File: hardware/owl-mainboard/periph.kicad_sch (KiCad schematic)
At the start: 38 parts, among them J301 AMOLED FPC, J302 LRA, J303 DOCK: GND, VBUS, DET, GND, U301 DRV2605LDGSR, U302 TMAG5273A2QDBVR, U303 LIS2DW12TR, U304 OPT3001DNPR, U305 LSF0204PWR, U306 XC6206P182MR

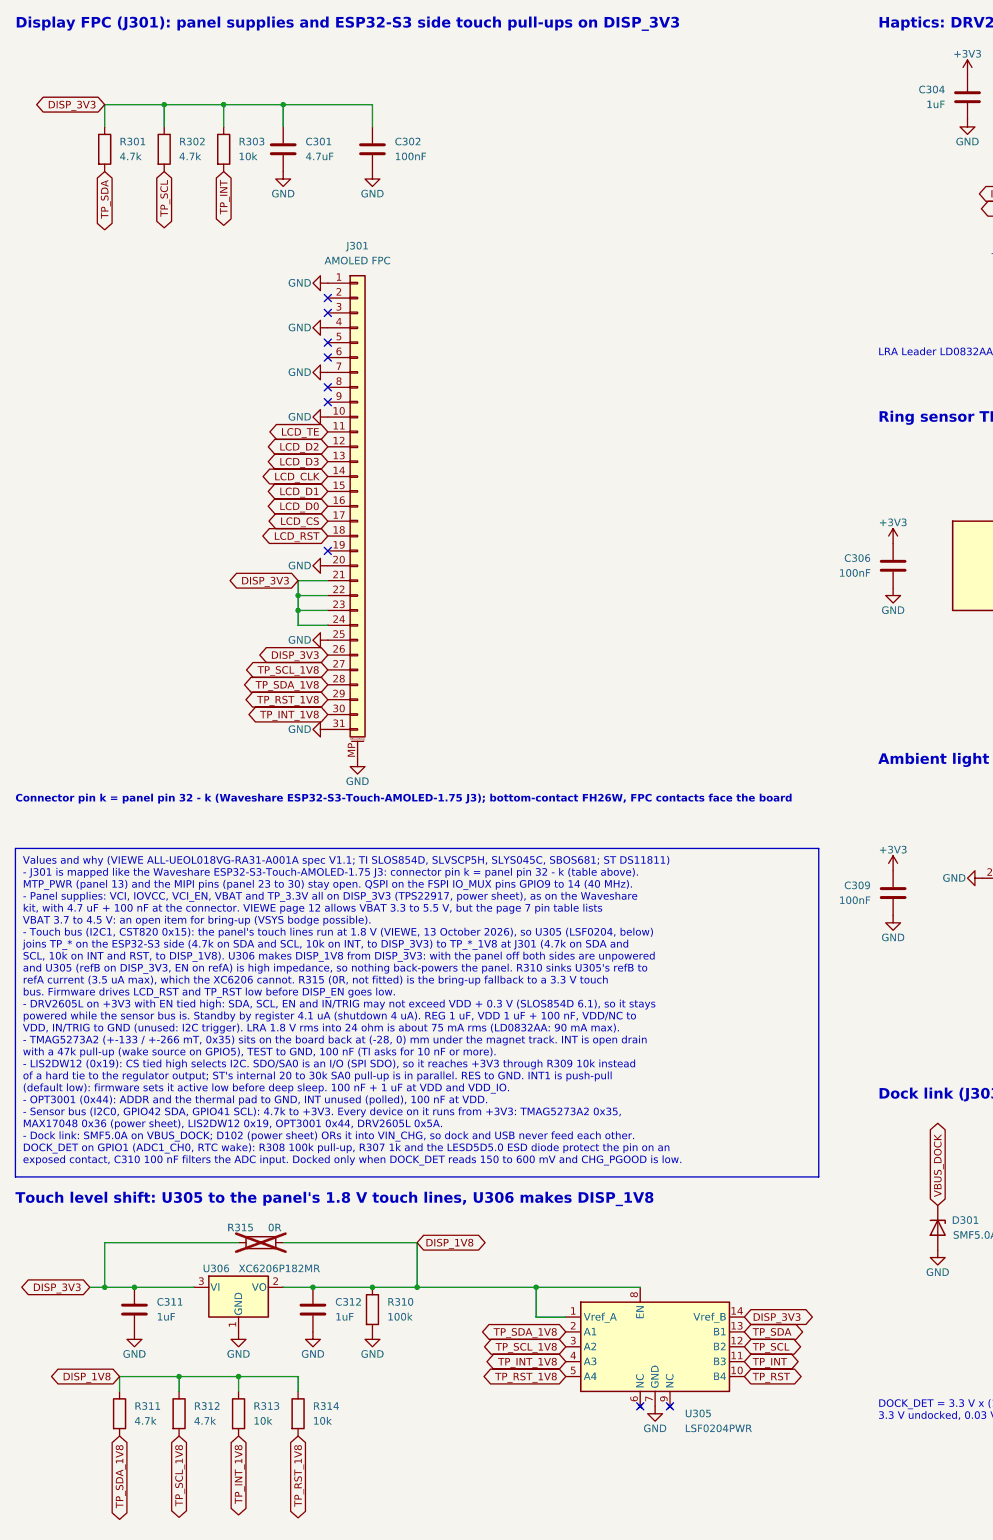
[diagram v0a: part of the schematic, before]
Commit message: feat(hardware): take the touch level shift off the periph sheet
U305, U306, C311, C312, R310 to R315 and their labels, wires and power
symbols go, with the "Touch level shift" heading and the LSF0204PWR and
XC6206 library symbols. J301 pins 27 to 30 carry TP_SCL, TP_SDA, TP_RST
and TP_INT again, in the labels and the J301 table.

The "Values and why" box gives the touch bus as 3.3 V logic with no
pull-ups in the panel and VBAT as 3.3 to 5.5 V (VIEWE's reply of 16
October 2026), and drops the level shift and R315 notes. The GPIO table
on mcu_usb no longer routes INT, RST and I2C1 through U305.

The main board's date moves to 2026-10-16, the day its design changed;
the schematics carry it, the PCB and its back silk follow with the board.
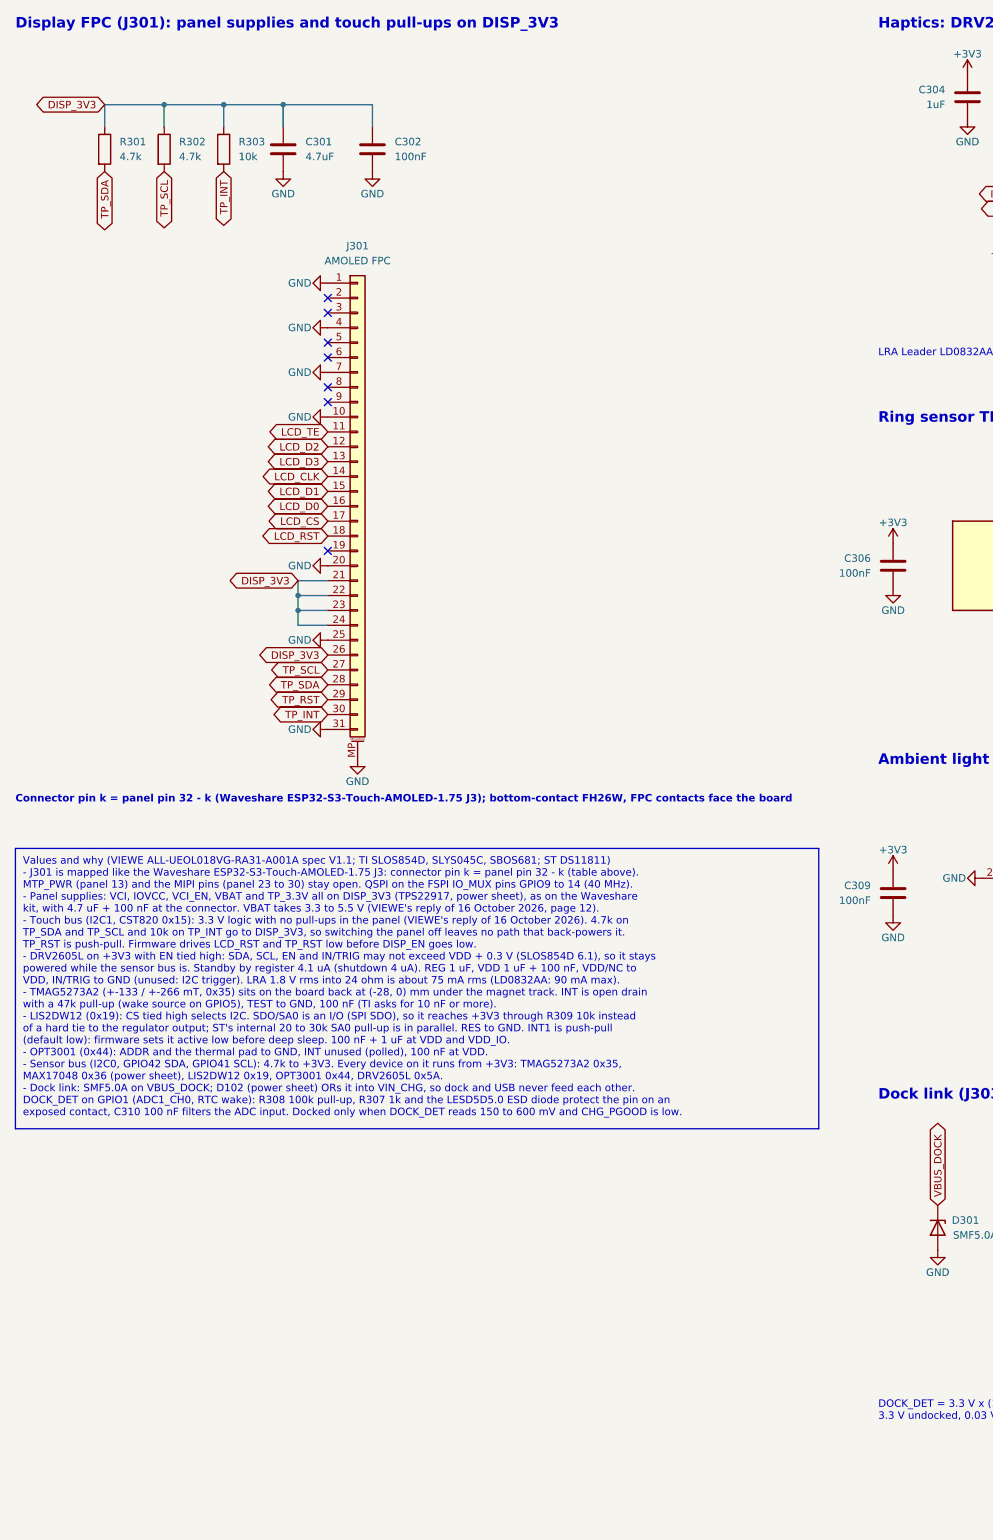
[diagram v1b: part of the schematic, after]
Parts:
- removed C311, C312: 1uF, Capacitor_SMD:C_0402_1005Metric, symbol Device:C
- removed R310: 100k, Resistor_SMD:R_0402_1005Metric, symbol Device:R
- removed R311, R312: 4.7k, Resistor_SMD:R_0402_1005Metric, symbol Device:R
- removed R313, R314: 10k, Resistor_SMD:R_0402_1005Metric, symbol Device:R
- removed R315: 0R, Resistor_SMD:R_0402_1005Metric, symbol Device:R
- removed U305: LSF0204PWR, Package_SO:TSSOP-14_4.4x5mm_P0.65mm, symbol owltunes:LSF0204PWR
- removed U306: XC6206P182MR, Package_TO_SOT_SMD:SOT-23-3, symbol Regulator_Linear:XC6206PxxxMR
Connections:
- net TP_INT_1V8 is gone; now on net TP_INT: J301.30 (Pin_30)
- net TP_RST_1V8 is gone; now on net TP_RST: J301.29 (Pin_29)
- net TP_SCL_1V8 is gone; now on net TP_SCL: J301.27 (Pin_27)
- net TP_SDA_1V8 is gone; now on net TP_SDA: J301.28 (Pin_28)
- no-connect marks 12 -> 10
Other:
- note added: "Display FPC (J301): panel supplies and touch pull-ups on DISP_3V3"
- note removed: "Display FPC (J301): panel supplies and ESP32-S3 side touch pull-ups on DISP_3V3"
- note removed: "Touch level shift: U305 to the panel's 1.8 V touch lines, U306 makes DISP_1V8"
